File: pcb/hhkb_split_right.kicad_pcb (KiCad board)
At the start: 2 copper layers, 173.7 x 97.4 mm, 92 parts, among them SW1 6, SW10 Y, SW11 U, SW12 I, SW13 O, SW14 P, SW15 [, SW16 ], SW17 Del, SW18 H, SW19 J, SW2 7, SW20 K, SW21 L, SW22 ;, SW23 ', SW24 Enter, SW25 N, SW26 M, SW27 ,, SW28 ., SW29 /, SW3 8, SW30 Shift, SW31 Fn, SW32 R-Space, SW33 Meta, SW34 Alt, SW4 9, SW5 0, SW6 -, SW7 =, SW8 \, SW9 `, U1 74LVC595, U2 74LVC595

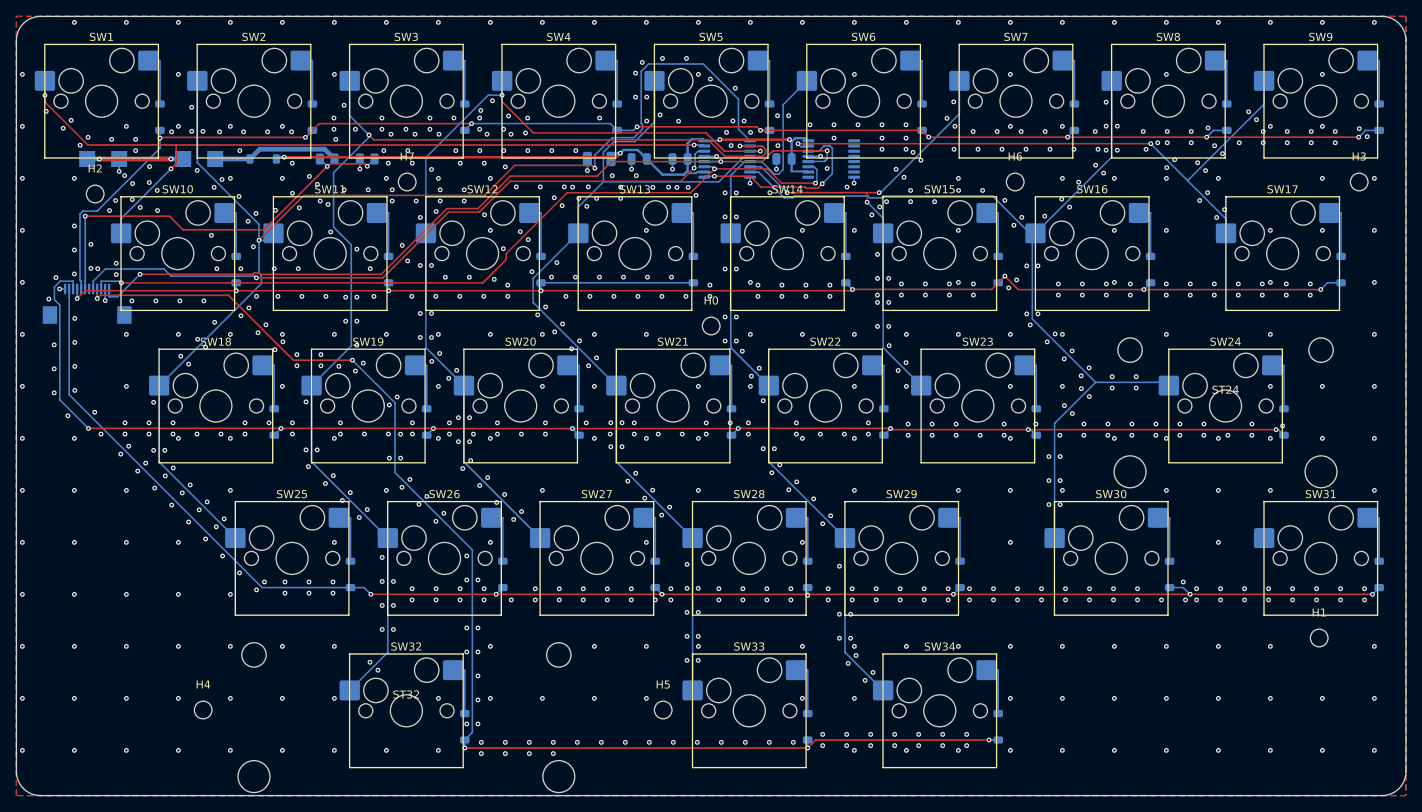
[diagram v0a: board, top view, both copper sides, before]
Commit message: DSNクリアランスマージンを左右共通15µmに確定（未配線 左0/右1）
利用者の要望「左右で違うマージン値を使う非対称は避けたい」に従い、
基板ごとに別マージンを使う案は取り下げ。**共通の値**で両基板の
未配線最小・DRC違反0を両立する値を総当たりで再探索した。

  M=15  左右とも DRC違反0。未配線は左右の Freerouting 実行タイミングで
        0〜2 の間で揺れる（同じ入力で 3 回実行して確認）。今回のコミット
        時点では 左0・右1（COL8-SW31、基板最遠端の列。過去の探索で
        構造的な残りと確認済み）

Freerouting 自身が打つビア（層間移動用）が規則ぎりぎりで他ネットに
近すぎることがあり、その 1 本を DRC の座標情報から直接押し出す
`gnd_fanout.nudge_tight_vias` を試作した。**失敗して撤回した。**
DRC の `pos` はアイテムの代表点であって実際の最近接距離ではないため、
「相手からの距離」を計算しても無関係な値になり、修正が一度も発火
しなかった（デバッグで dist=1.088mm という無意味な値を確認）。
この方式では直せない。実装は削除済み。

Co-Authored-By: Claude Sonnet 5 <noreply@anthropic.com>
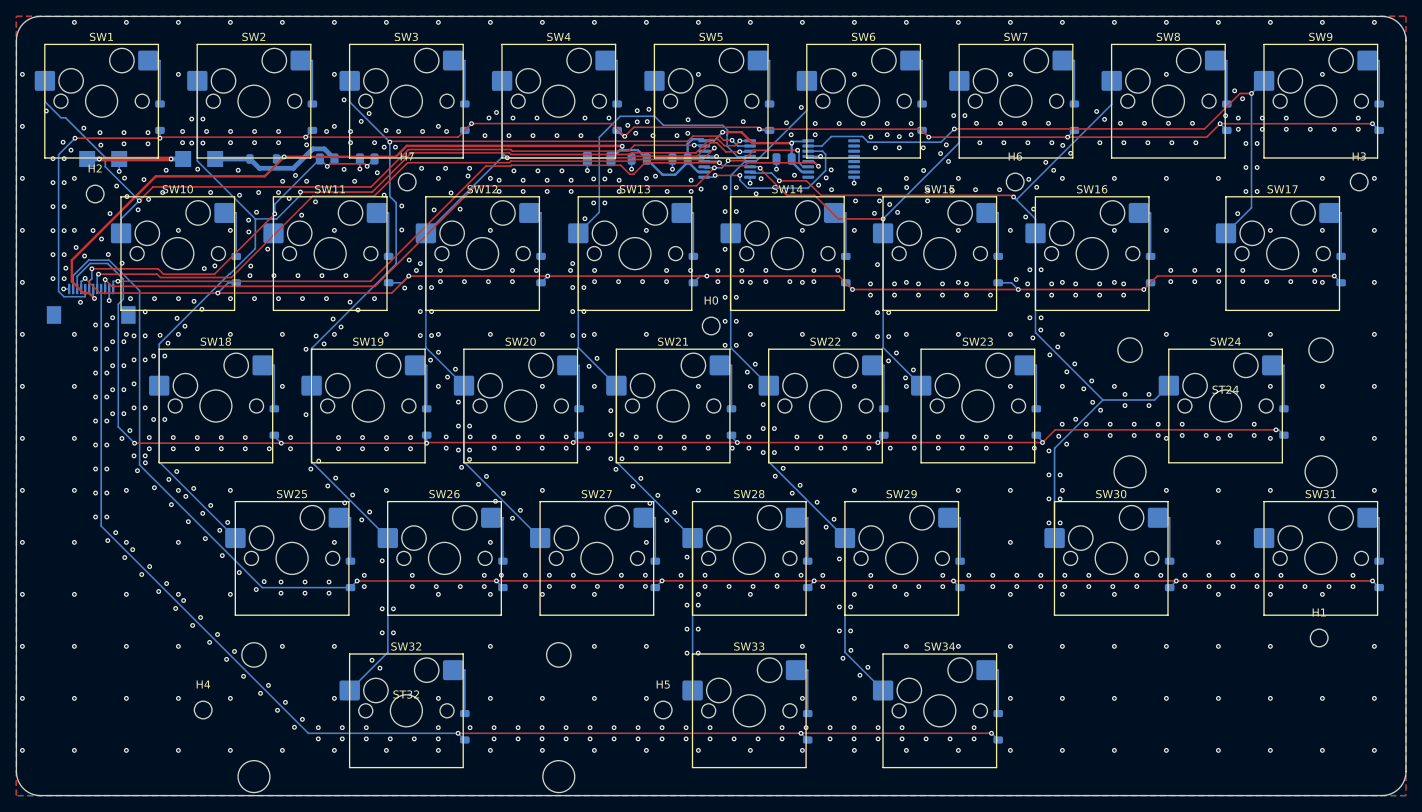
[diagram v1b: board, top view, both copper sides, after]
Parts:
- moved J_DB 0.50 mm to (72.5, 87.2)
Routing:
- net V3V3: track 82.2 -> 122.4 mm, vias 4 -> 5
- net COL1: track 154.3 -> 137.8 mm
- net ROW0: track 188.4 -> 200.6 mm, vias 9 -> 10
- net ROW1: track 187.0 -> 176.1 mm, vias 8 -> 9
- net COL2: track 143.9 -> 134.8 mm
- net COL4: track 111.9 -> 103.9 mm
- net ROW3: track 195.2 -> 202.0 mm
- net COL3: track 105.0 -> 99.4 mm
- net VBATT_SENSE: track 51.2 -> 46.0 mm, vias 3 -> 4
- net ROW4: track 159.8 -> 155.2 mm, vias 5 -> 3
- net COL5: track 92.8 -> 88.8 mm
- net CS: track 104.0 -> 100.2 mm
- net COL8: track 77.1 -> 79.7 mm
- net U1_U2: track 24.0 -> 21.5 mm
- net COL7: track 115.2 -> 112.8 mm, vias 0 -> 2
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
